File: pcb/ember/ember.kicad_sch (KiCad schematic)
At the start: 33 parts, among them J2 USB_C_Receptacle_USB2.0, SW1 RESET, SW2 BOOT, U33 AMS1117-3.3, Y1 16MHz

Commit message: :wrench: ver1.1
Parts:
- removed D1: D_TVS_Dual_AAC, Package_TO_SOT_SMD:SOT-23, symbol Device:D_TVS_Dual_AAC
- removed TP1: SWCLK, TestPoint:TestPoint_THTPad_D1.0mm_Drill0.5mm, symbol Connector:TestPoint
- removed TP2: GND, TestPoint:TestPoint_THTPad_D1.0mm_Drill0.5mm, symbol Connector:TestPoint
- removed TP3: SWDIO, TestPoint:TestPoint_THTPad_D1.0mm_Drill0.5mm, symbol Connector:TestPoint
- removed TP4: RESET, TestPoint:TestPoint_THTPad_D1.0mm_Drill0.5mm, symbol Connector:TestPoint
- added J1: Conn_01x04_Socket, Connector_PinSocket_2.54mm:PinSocket_1x04_P2.54mm_Vertical, symbol Connector:Conn_01x04_Socket
- added U34: SRV05-4, Package_TO_SOT_SMD:SOT-23-6, symbol Power_Protection:SRV05-4
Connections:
- net +5V: now also U34.5 (VP)
- net GND: now also J1.2 (Pin_2), U34.2 (VN)
- net NRST: now also J1.4 (Pin_4)
- net SWCLK: now also J1.1 (Pin_1)
- net SWDIO: now also J1.3 (Pin_3)
- net USB_D+: now also U34.6 (IO4)
- net USB_D-: now also U34.4 (IO3)

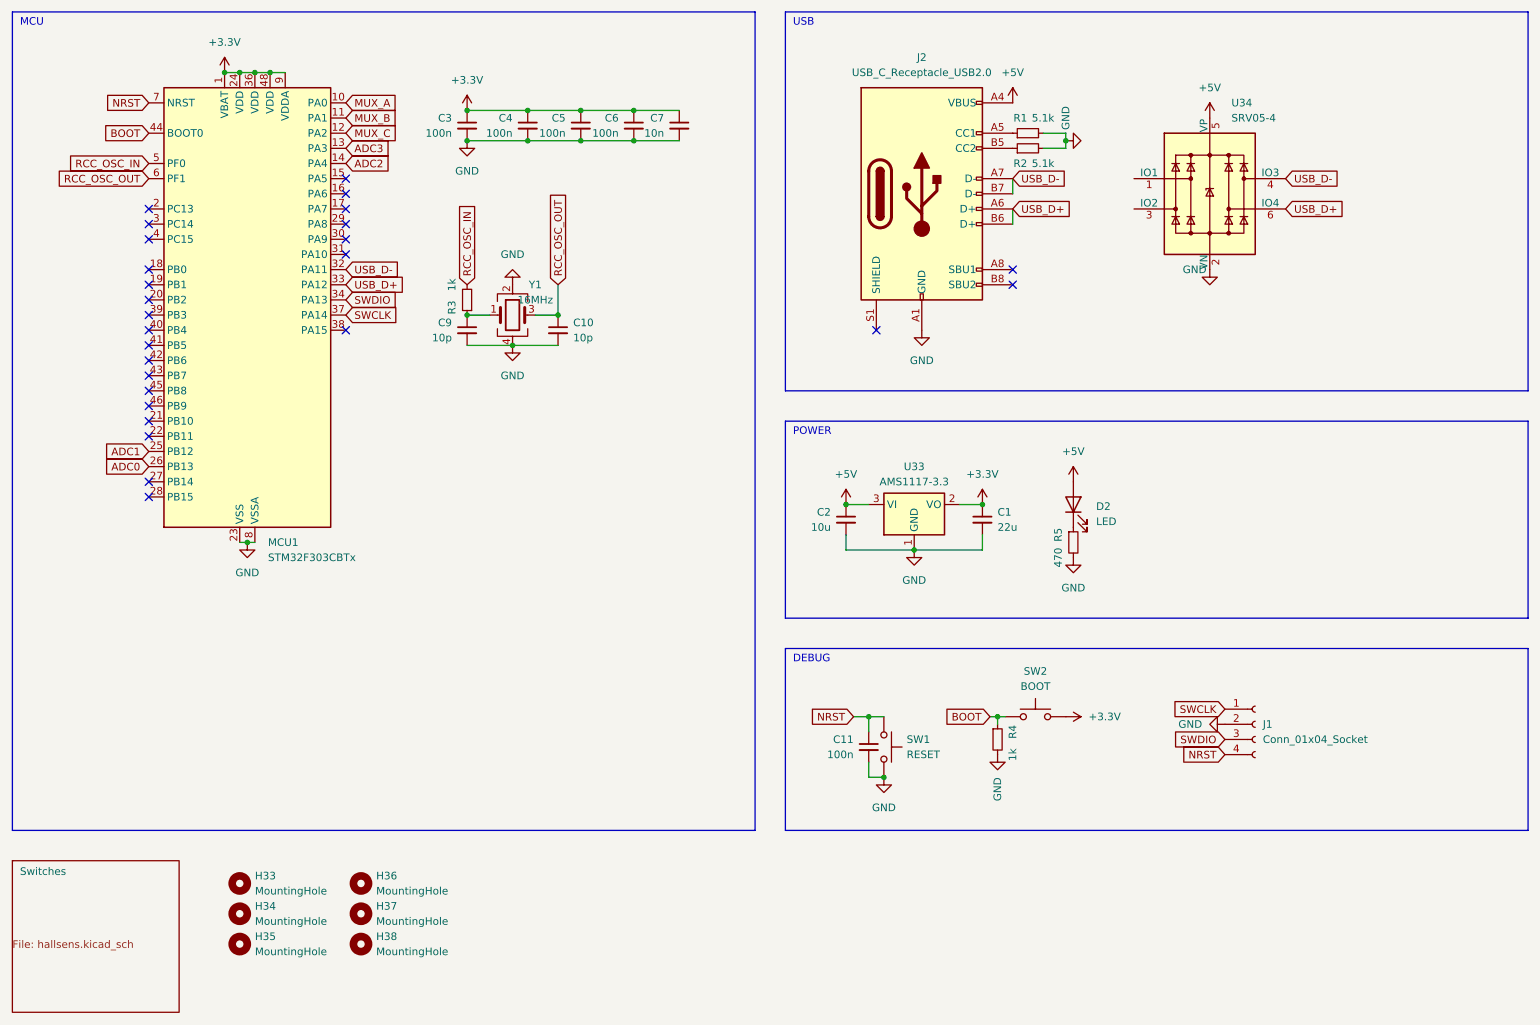
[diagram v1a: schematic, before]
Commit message: :sparkles: add eeprom
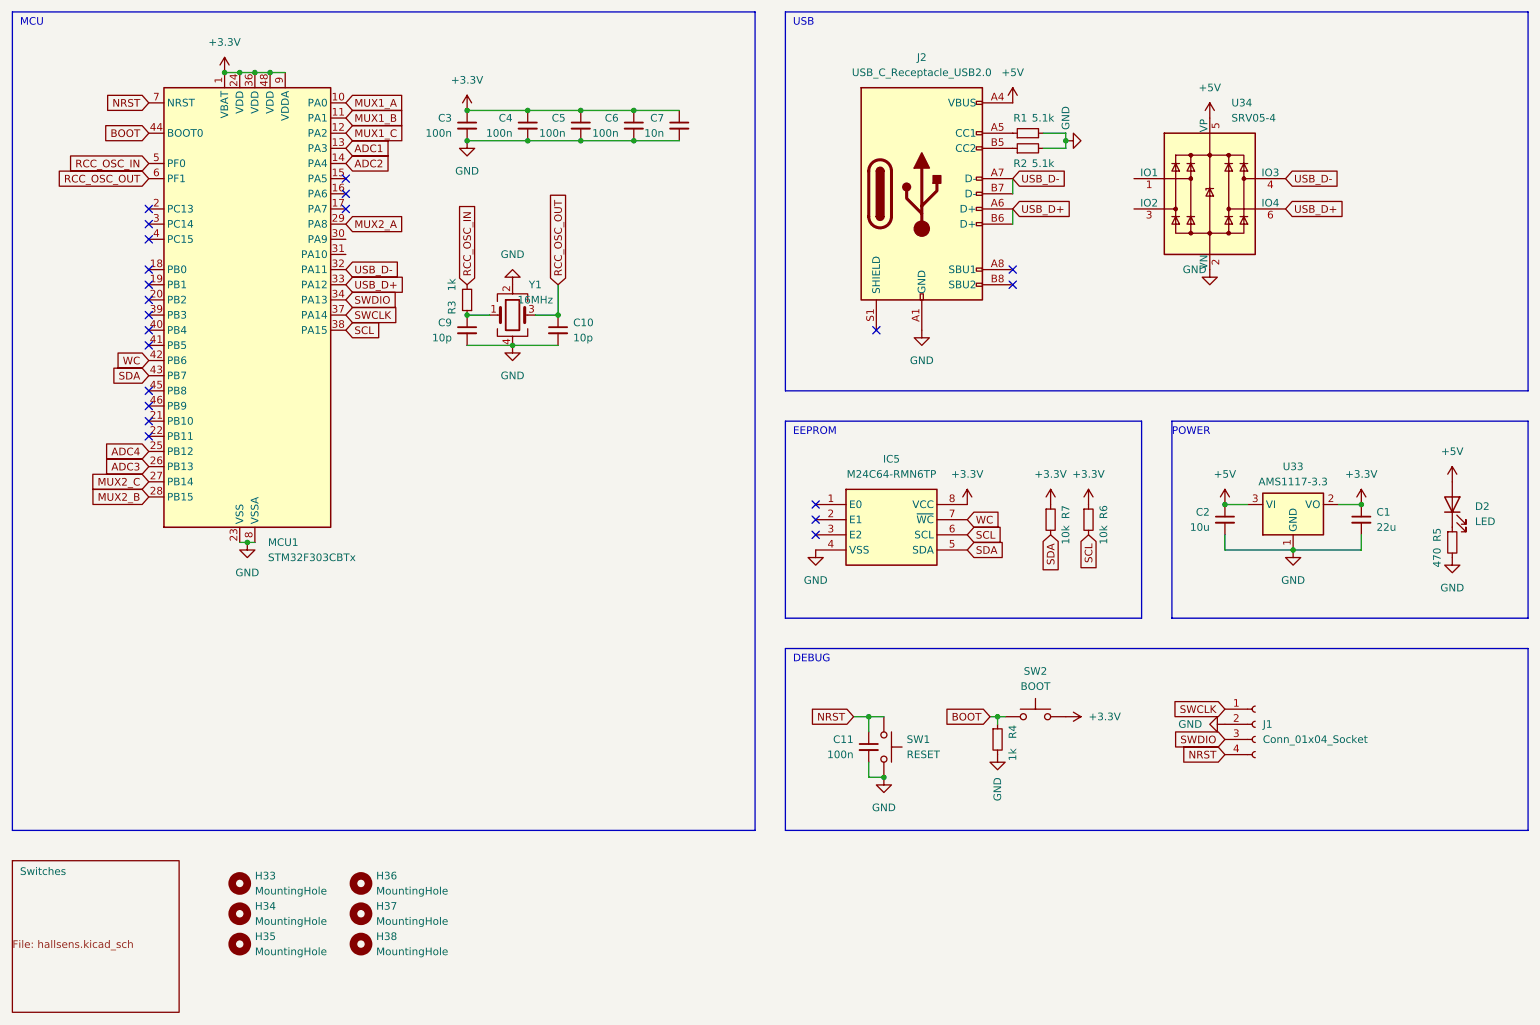
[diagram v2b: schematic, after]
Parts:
- added IC5: M24C64-RMN6TP, SOIC127P600X175-8N, symbol ember_m24c64:M24C64-RMN6TP
- added R6, R7: 10k, Resistor_SMD:R_0603_1608Metric, symbol Device:R_Small
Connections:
- net ADC0 is gone; now on net ADC3: MCU1.26 (PB13)
- net +3.3V: now also IC5.8 (VCC), R6.1, R7.1
- net ADC1: now also MCU1.13 (PA3); no longer MCU1.25 (PB12)
- net ADC3: no longer MCU1.13 (PA3)
- net GND: now also IC5.4 (VSS)
- net MUX2_C: now reaches MCU1.27 (PB14)
- net MUX2_B: now reaches MCU1.28 (PB15)
- net MUX2_A: now reaches MCU1.29 (PA8)
- net SCL: now reaches MCU1.38 (PA15)
- net SCL: now also IC5.6 (SCL), R6.2
- net WC: now reaches MCU1.42 (PB6)
- net WC: now also IC5.7 (~{WC})
- net SDA: now reaches MCU1.43 (PB7)
- net SDA: now also IC5.5 (SDA), R7.2
- net MUX_A renamed MUX1_A
- net MUX_B renamed MUX1_B
- net MUX_C renamed MUX1_C
- new net ADC4: MCU1.25 (PB12)
- no-connect marks 27 -> 22
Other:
- note added: "EEPROM"
- moved on the sheet: C1, C2, D2, R5, U33

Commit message: :bug: add 1.5k pullup to D+
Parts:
- added R8: 1.5k, Resistor_SMD:R_0603_1608Metric, symbol Device:R_Small
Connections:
- net +3.3V: now also R8.2
- net USB_D+: now also R8.1
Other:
- moved on the sheet: U34
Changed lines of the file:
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@@
     )
   )
-  (global_label "USB_D+" (shape input) (at 238.76 58.42 0) (fields_autoplaced)
+  (global_label "USB_D+" (shape input) (at 254 59.69 0) (fields_autoplaced)
     (effects (font (size 1.27 1.27)) (justify left))
-    (property "Intersheetrefs" "${INTERSHEET_REFS}" (at 249.3652 58.42 0)
+    (property "Intersheetrefs" "${INTERSHEET_REFS}" (at 264.6052 59.69 0)
       (effects (font (size 1.27 1.27)) (justify left) hide)
     )
@@
     )
   )
+  (global_label "USB_D+" (shape input) (at 215.9 58.42 270) (fields_autoplaced)
+    (effects (font (size 1.27 1.27)) (justify right))
+    (property "Intersheetrefs" "${INTERSHEET_REFS}" (at 215.9 69.0252 90)
+      (effects (font (size 1.27 1.27)) (justify right) hide)
+    )
+  )
   (global_label "SDA" (shape input) (at 199.39 113.03 270) (fields_autoplaced)
     (effects (font (size 1.27 1.27)) (justify right))
@@
     )
   )
-  (global_label "USB_D-" (shape input) (at 238.76 53.34 0) (fields_autoplaced)
+  (global_label "USB_D-" (shape input) (at 254 54.61 0) (fields_autoplaced)
     (effects (font (size 1.27 1.27)) (justify left))
-    (property "Intersheetrefs" "${INTERSHEET_REFS}" (at 249.3652 53.34 0)
+    (property "Intersheetrefs" "${INTERSHEET_REFS}" (at 264.6052 54.61 0)
       (effects (font (size 1.27 1.27)) (justify left) hide)
     )
@@
     )
   )
-  (symbol (lib_id "Power_Protection:SRV05-4") (at 226.06 55.88 0) (unit 1)
-    (in_bom yes) (on_board yes) (dnp no) (fields_autoplaced)
-    (property "Reference" "U34" (at 229.6861 40.64 0)
-      (effects (font (size 1.27 1.27)) (justify left))
-    )
-    (property "Value" "SRV05-4" (at 229.6861 43.18 0)
-      (effects (font (size 1.27 1.27)) (justify left))
-    )
-    (property "Footprint" "Package_TO_SOT_SMD:SOT-23-6" (at 243.84 67.31 0)
-      (effects (font (size 1.27 1.27)) hide)
-    )
-    (property "Datasheet" "http://www.onsemi.com/pub/Collateral/SRV05-4-D.PDF" (at 226.06 55.88 0)
-      (effects (font (size 1.27 1.27)) hide)
-    )
-    (property "LCSC" "C85364" (at 226.06 55.88 0)
+  (symbol (lib_id "Power_Protection:SRV05-4") (at 241.3 57.15 0) (unit 1)
+    (in_bom yes) (on_board yes) (dnp no) (fields_autoplaced)
+    (property "Reference" "U34" (at 244.9261 41.91 0)
+      (effects (font (size 1.27 1.27)) (justify left))
+    )
+    (property "Value" "SRV05-4" (at 244.9261 44.45 0)
+      (effects (font (size 1.27 1.27)) (justify left))
+    )
+    (property "Footprint" "Package_TO_SOT_SMD:SOT-23-6" (at 259.08 68.58 0)
+      (effects (font (size 1.27 1.27)) hide)
+    )
+    (property "Datasheet" "http://www.onsemi.com/pub/Collateral/SRV05-4-D.PDF" (at 241.3 57.15 0)
+      (effects (font (size 1.27 1.27)) hide)
+    )
+    (property "LCSC" "C85364" (at 241.3 57.15 0)
       (effects (font (size 1.27 1.27)) hide)
     )
@@
     )
   )
+  (symbol (lib_id "Device:R_Small") (at 215.9 55.88 180) (unit 1)
+    (in_bom yes) (on_board yes) (dnp no)
+    (property "Reference" "R8" (at 218.44 57.15 90)
+      (effects (font (size 1.27 1.27)))
+    )
+    (property "Value" "1.5k" (at 218.44 53.34 90)
+      (effects (font (size 1.27 1.27)))
+    )
+    (property "Footprint" "Resistor_SMD:R_0603_1608Metric" (at 215.9 55.88 0)
+      (effects (font (size 1.27 1.27)) hide)
+    )
+    (property "Datasheet" "~" (at 215.9 55.88 0)
+      (effects (font (size 1.27 1.27)) hide)
+    )
+    (property "LCSC" "C22843" (at 215.9 55.88 90)
+      (effects (font (size 1.27 1.27)) hide)
+    )
+    (pin "1")
+    (pin "2")
+    (instances
+      (project "ember"
+        (path "/677b9f05-bf95-4903-b139-ff3eec86ab18"
+          (reference "R8") (unit 1)
+        )
+      )
+    )
+  )
   (symbol (lib_id "Device:R_Small") (at 195.58 45.72 90) (unit 1)
     (in_bom yes) (on_board yes) (dnp no)
@@
         (path "/677b9f05-bf95-4903-b139-ff3eec86ab18"
           (reference "D2") (unit 1)
+        )
+      )
+    )
+  )
+  (symbol (lib_id "power:+3.3V") (at 215.9 53.34 0) (unit 1)
+    (in_bom yes) (on_board yes) (dnp no) (fields_autoplaced)
+    (property "Reference" "#PWR041" (at 215.9 57.15 0)
+      (effects (font (size 1.27 1.27)) hide)
+    )
+    (property "Value" "+3.3V" (at 215.9 48.26 0)
+      (effects (font (size 1.27 1.27)))
+    )
+    (property "Footprint" "" (at 215.9 53.34 0)
+      (effects (font (size 1.27 1.27)) hide)
+    )
+    (property "Datasheet" "" (at 215.9 53.34 0)
+      (effects (font (size 1.27 1.27)) hide)
+    )
+    (pin "1")
+    (instances
+      (project "ember"
+        (path "/677b9f05-bf95-4903-b139-ff3eec86ab18"
+          (reference "#PWR041") (unit 1)
         )
       )
@@
     )
   )
-  (symbol (lib_id "power:+5V") (at 226.06 43.18 0) (unit 1)
-    (in_bom yes) (on_board yes) (dnp no) (fields_autoplaced)
-    (property "Reference" "#PWR037" (at 226.06 46.99 0)
-      (effects (font (size 1.27 1.27)) hide)
-    )
-    (property "Value" "+5V" (at 226.06 38.1 0)
-      (effects (font (size 1.27 1.27)))
-    )
-    (property "Footprint" "" (at 226.06 43.18 0)
-      (effects (font (size 1.27 1.27)) hide)
-    )
-    (property "Datasheet" "" (at 226.06 43.18 0)
+  (symbol (lib_id "power:+5V") (at 241.3 44.45 0) (unit 1)
+    (in_bom yes) (on_board yes) (dnp no) (fields_autoplaced)
+    (property "Reference" "#PWR037" (at 241.3 48.26 0)
+      (effects (font (size 1.27 1.27)) hide)
+    )
+    (property "Value" "+5V" (at 241.3 39.37 0)
+      (effects (font (size 1.27 1.27)))
+    )
+    (property "Footprint" "" (at 241.3 44.45 0)
+      (effects (font (size 1.27 1.27)) hide)
+    )
+    (property "Datasheet" "" (at 241.3 44.45 0)
       (effects (font (size 1.27 1.27)) hide)
     )
@@
     )
   )
-  (symbol (lib_id "power:GND") (at 226.06 68.58 0) (unit 1)
-    (in_bom yes) (on_board yes) (dnp no)
-    (property "Reference" "#PWR036" (at 226.06 74.93 0)
-      (effects (font (size 1.27 1.27)) hide)
-    )
-    (property "Value" "GND" (at 223.52 68.58 0)
-      (effects (font (size 1.27 1.27)))
-    )
-    (property "Footprint" "" (at 226.06 68.58 0)
-      (effects (font (size 1.27 1.27)) hide)
-    )
-    (property "Datasheet" "" (at 226.06 68.58 0)
-      (effects (font (size 1.27 1.27)) hide)
-    )
+  (symbol (lib_id "power:GND") (at 241.3 69.85 0) (unit 1)
+    (in_bom yes) (on_board yes) (dnp no)
+    (property "Reference" "#PWR036" (at 241.3 76.2 0)
+      (effects (font (size 1.27 1.27)) hide)
+    )
+    (property "Value" "GND" (at 238.76 69.85 0)
+      (effects (font (size 1.27 1.27)))
+    )
+    (property "Footprint" "" (at 241.3 69.85 0)
+      (effects (font (size 1.27 1.27)) hide)
+    )
+    (property "Datasheet" "" (at 241.3 69.85 0)
+      (effects (font (size 1.27 1.27)) hide)
+    )
